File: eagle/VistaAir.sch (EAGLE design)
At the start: 11 parts, among them IC1 MCP170312MB, J1 POWER_JACK

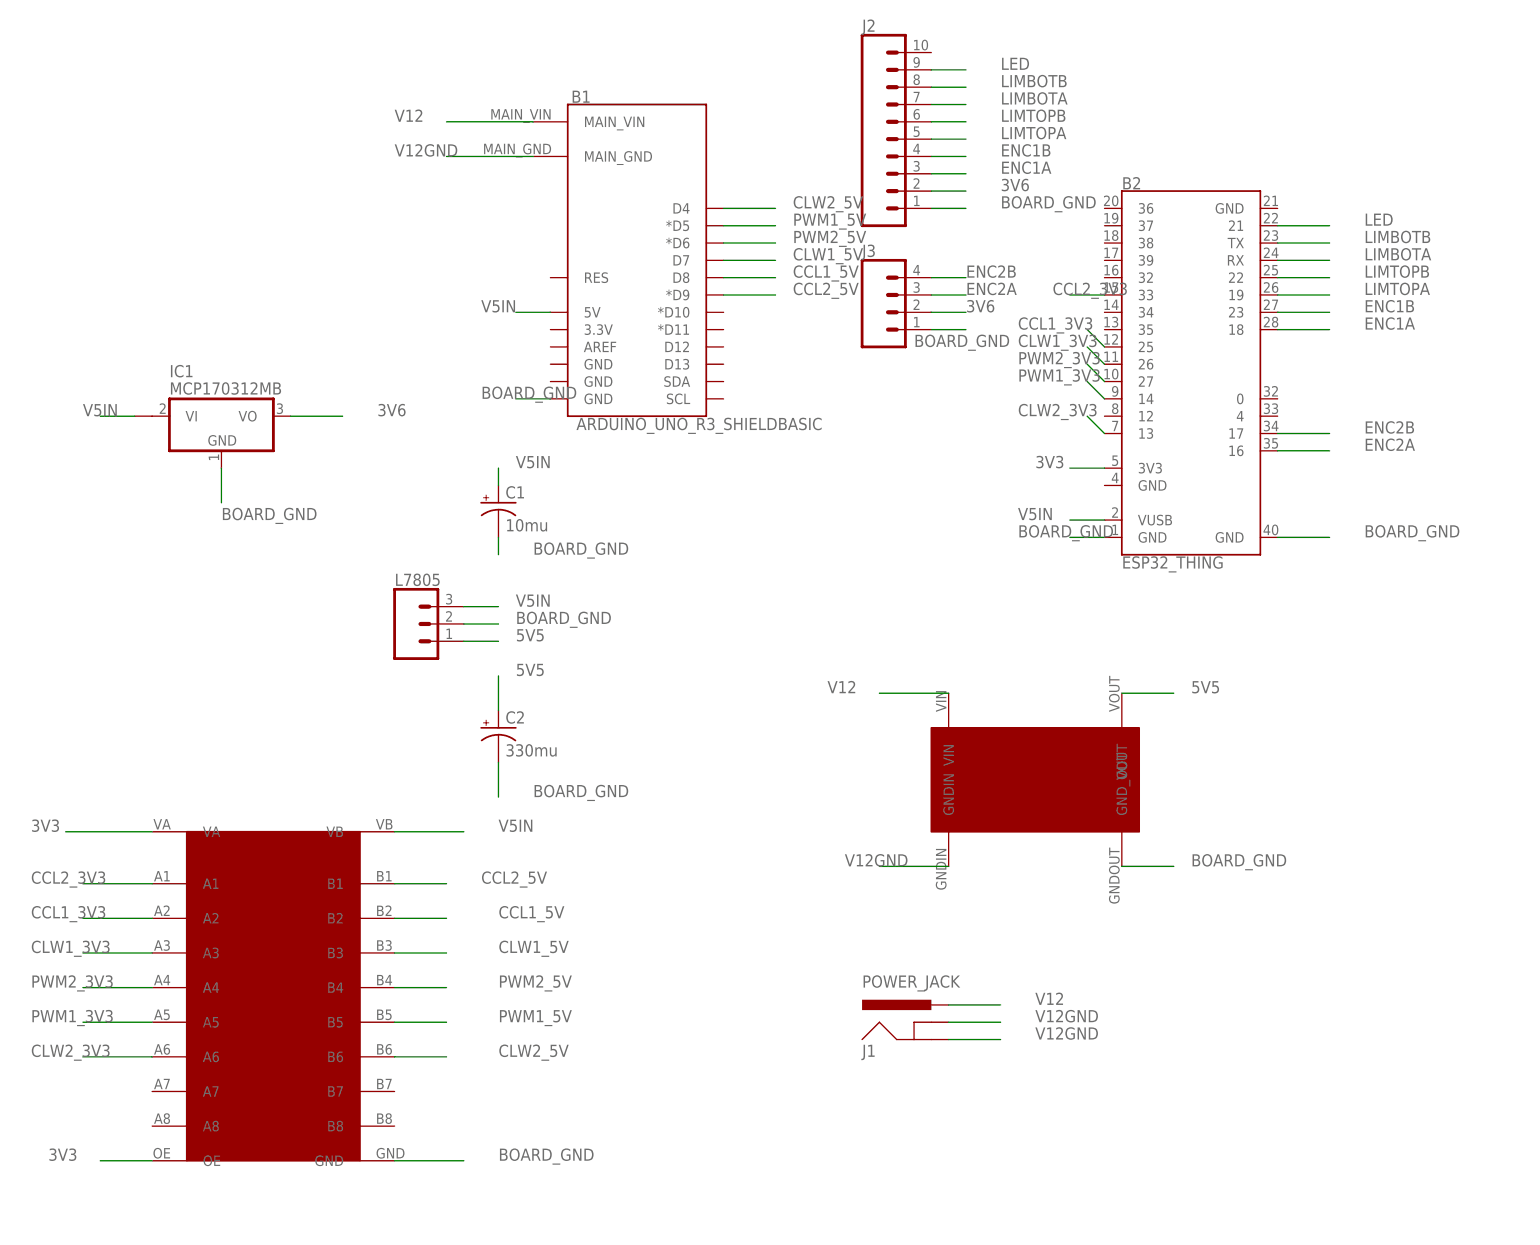
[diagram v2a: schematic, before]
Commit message: using one way logic translator since motor driver PWM inputs are open drain - and sets up ultra-high-frequency push pull with bi-directional logic shifter
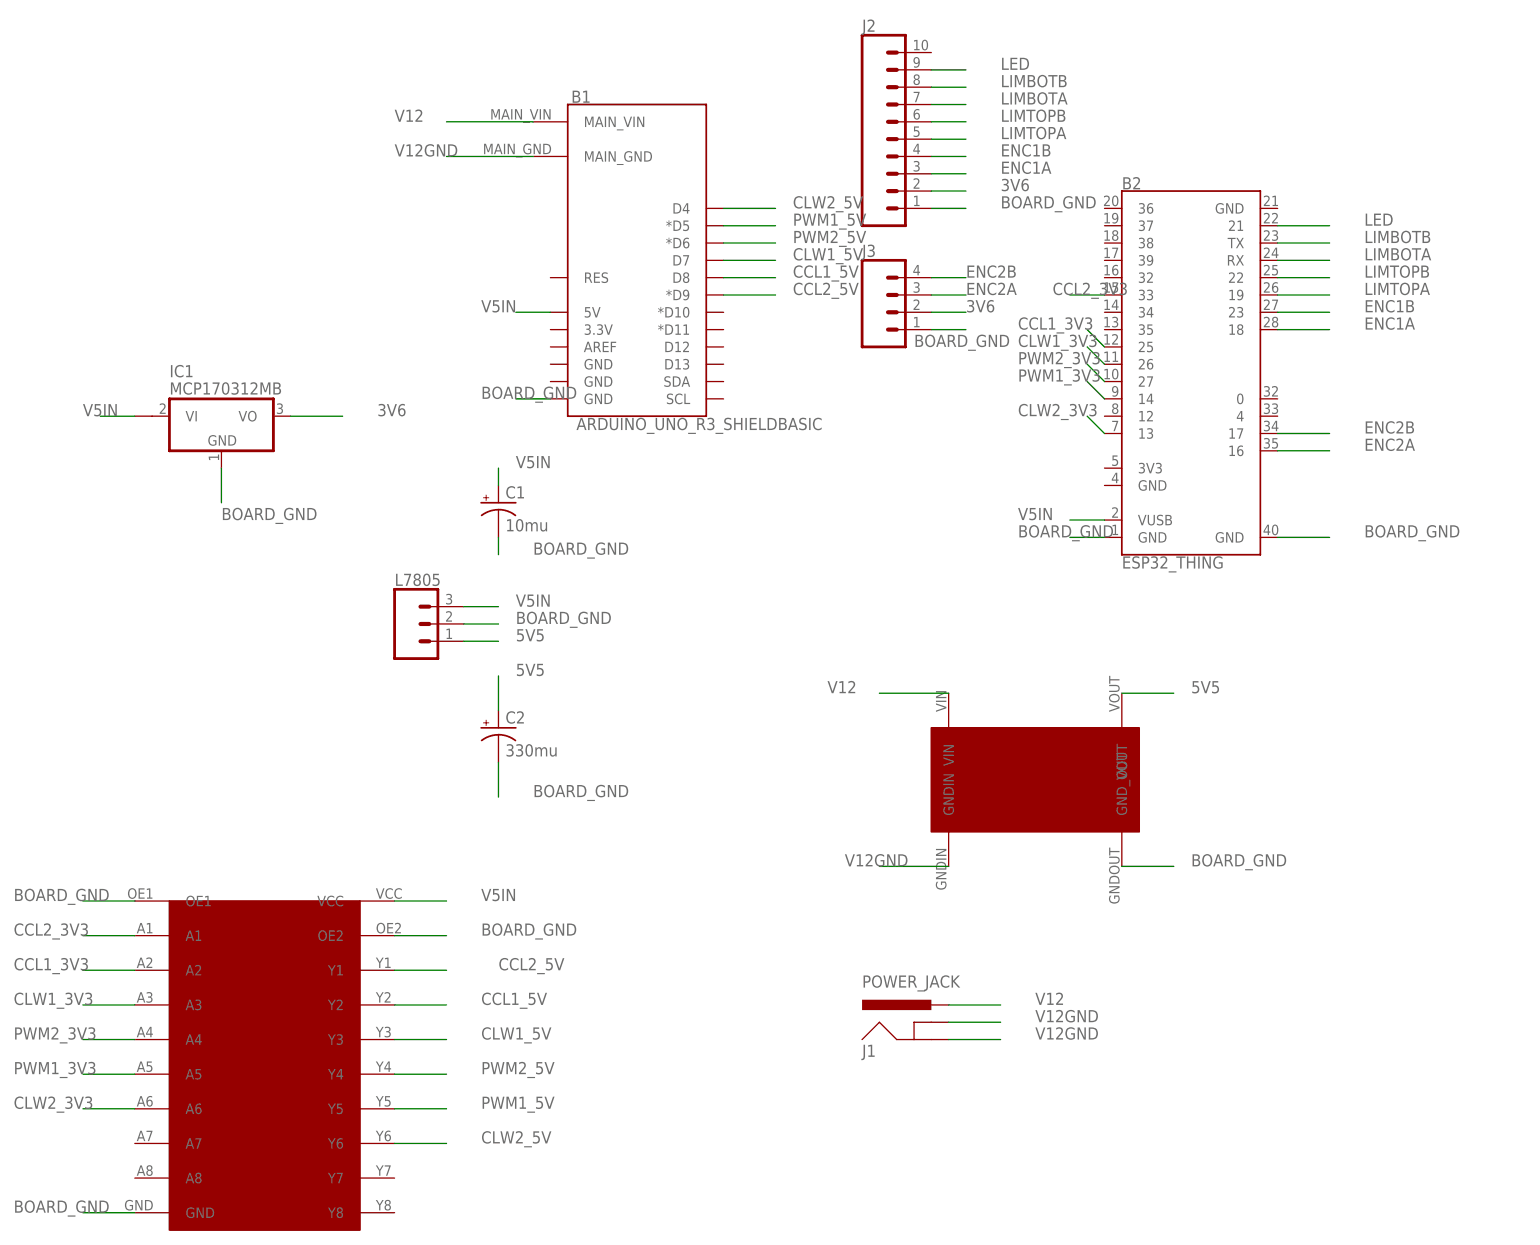
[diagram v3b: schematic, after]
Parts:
- removed U$3: 8_CHANNEL_LOGIC_CONVERTER, kevins_parts:8_CHANNEL_LOGIC_CONVERTER
- added U$1: SN74AHCT541_SOIC-20, kevins_parts:SN74AHCT541_SOIC-20
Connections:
- removed net 3V3: B2.3V3@5, U$3.OE, U$3.VA
- net BOARD_GND: now also U$1.GND, U$1.OE1, U$1.OE2; no longer U$3.GND
- net CCL1_3V3: now also U$1.A2; no longer U$3.A2
- net CCL1_5V: now also U$1.Y2; no longer U$3.B2
- net CCL2_3V3: now also U$1.A1; no longer U$3.A1
- net CCL2_5V: now also U$1.Y1; no longer U$3.B1
- net CLW1_3V3: now also U$1.A3; no longer U$3.A3
- net CLW1_5V: now also U$1.Y3; no longer U$3.B3
- net CLW2_3V3: now also U$1.A6; no longer U$3.A6
- net CLW2_5V: now also U$1.Y6; no longer U$3.B6
- net PWM1_3V3: now also U$1.A5; no longer U$3.A5
- net PWM1_5V: now also U$1.Y5; no longer U$3.B5
- net PWM2_3V3: now also U$1.A4; no longer U$3.A4
- net PWM2_5V: now also U$1.Y4; no longer U$3.B4
- net V5IN: now also U$1.VCC; no longer U$3.VB
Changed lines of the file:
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@@
 <part name="C1" library="adafruit" deviceset="CPOL-US" device="TT2D5" value="10mu"/>
 <part name="U$2" library="kevins_parts" deviceset="LM2596_STEPDOWN_MODULE" device=""/>
-<part name="U$3" library="kevins_parts" deviceset="8_CHANNEL_LOGIC_CONVERTER" device=""/>
 <part name="IC1" library="linear" deviceset="MCP1703*" device="MB" technology="12"/>
 <part name="J1" library="SparkFun-Connectors" deviceset="POWER_JACK" device=""/>
+<part name="U$1" library="kevins_parts" deviceset="SN74AHCT541_SOIC-20" device=""/>
 </parts>
 <sheets>
@@
 <instance part="C1" gate="G$1" x="25.4" y="40.64"/>
 <instance part="U$2" gate="G$1" x="99.06" y="-27.94" rot="R270"/>
-<instance part="U$3" gate="G$1" x="5.08" y="-35.56"/>
 <instance part="IC1" gate="G$1" x="-15.24" y="53.34"/>
 <instance part="J1" gate="G$1" x="88.9" y="-40.64"/>
+<instance part="U$1" gate="G$1" x="2.54" y="-43.18"/>
 </instances>
 <busses>
@@
 <net name="CLW1_3V3" class="0">
 <segment>
-<pinref part="U$3" gate="G$1" pin="A3"/>
-<wire x1="-25.4" y1="-25.4" x2="-35.56" y2="-25.4" width="0.1524" layer="91"/>
-<label x="-43.18" y="-25.4" size="1.778" layer="95"/>
-</segment>
-<segment>
 <wire x1="114.3" y1="60.96" x2="111.76" y2="63.5" width="0.1524" layer="91"/>
 <label x="101.6" y="63.5" size="1.778" layer="95"/>
 <pinref part="B2" gate="G$1" pin="26"/>
 </segment>
+<segment>
+<pinref part="U$1" gate="G$1" pin="A3"/>
+<wire x1="-27.94" y1="-33.02" x2="-35.56" y2="-33.02" width="0.1524" layer="91"/>
+<label x="-45.72" y="-33.02" size="1.778" layer="95"/>
+</segment>
 </net>
 <net name="PWM2_3V3" class="0">
-<segment>
-<pinref part="U$3" gate="G$1" pin="A4"/>
-<wire x1="-25.4" y1="-30.48" x2="-35.56" y2="-30.48" width="0.1524" layer="91"/>
-<label x="-43.18" y="-30.48" size="1.778" layer="95"/>
-</segment>
 <segment>
 <wire x1="114.3" y1="58.42" x2="111.76" y2="60.96" width="0.1524" layer="91"/>
@@
 <pinref part="B2" gate="G$1" pin="27"/>
 </segment>
+<segment>
+<pinref part="U$1" gate="G$1" pin="A4"/>
+<wire x1="-27.94" y1="-38.1" x2="-35.56" y2="-38.1" width="0.1524" layer="91"/>
+<label x="-45.72" y="-38.1" size="1.778" layer="95"/>
+</segment>
 </net>
 <net name="PWM1_3V3" class="0">
-<segment>
-<pinref part="U$3" gate="G$1" pin="A5"/>
-<wire x1="-25.4" y1="-35.56" x2="-35.56" y2="-35.56" width="0.1524" layer="91"/>
-<label x="-43.18" y="-35.56" size="1.778" layer="95"/>
-</segment>
 <segment>
 <wire x1="114.3" y1="55.88" x2="111.76" y2="58.42" width="0.1524" layer="91"/>
@@
 <pinref part="B2" gate="G$1" pin="14"/>
 </segment>
+<segment>
+<pinref part="U$1" gate="G$1" pin="A5"/>
+<wire x1="-27.94" y1="-43.18" x2="-35.56" y2="-43.18" width="0.1524" layer="91"/>
+<label x="-45.72" y="-43.18" size="1.778" layer="95"/>
+</segment>
 </net>
 <net name="CLW2_3V3" class="0">
@@
 </segment>
 <segment>
-<pinref part="U$3" gate="G$1" pin="A6"/>
-<wire x1="-25.4" y1="-40.64" x2="-35.56" y2="-40.64" width="0.1524" layer="91"/>
-<label x="-43.18" y="-40.64" size="1.778" layer="95"/>
+<pinref part="U$1" gate="G$1" pin="A6"/>
+<wire x1="-27.94" y1="-48.26" x2="-35.56" y2="-48.26" width="0.1524" layer="91"/>
+<label x="-45.72" y="-48.26" size="1.778" layer="95"/>
 </segment>
 </net>
 <net name="CCL1_3V3" class="0">
-<segment>
-<pinref part="U$3" gate="G$1" pin="A2"/>
-<wire x1="-25.4" y1="-20.32" x2="-35.56" y2="-20.32" width="0.1524" layer="91"/>
-<label x="-43.18" y="-20.32" size="1.778" layer="95"/>
-</segment>
 <segment>
 <wire x1="114.3" y1="63.5" x2="111.76" y2="66.04" width="0.1524" layer="91"/>
@@
 <pinref part="B2" gate="G$1" pin="25"/>
 </segment>
+<segment>
+<pinref part="U$1" gate="G$1" pin="A2"/>
+<wire x1="-27.94" y1="-27.94" x2="-35.56" y2="-27.94" width="0.1524" layer="91"/>
+<label x="-45.72" y="-27.94" size="1.778" layer="95"/>
+</segment>
 </net>
 <net name="CCL2_3V3" class="0">
-<segment>
-<pinref part="U$3" gate="G$1" pin="A1"/>
-<wire x1="-25.4" y1="-15.24" x2="-35.56" y2="-15.24" width="0.1524" layer="91"/>
-<label x="-43.18" y="-15.24" size="1.778" layer="95"/>
-</segment>
 <segment>
 <pinref part="B2" gate="G$1" pin="33"/>
@@
 <label x="106.68" y="71.12" size="1.778" layer="95"/>
 </segment>
+<segment>
+<pinref part="U$1" gate="G$1" pin="A1"/>
+<wire x1="-27.94" y1="-22.86" x2="-35.56" y2="-22.86" width="0.1524" layer="91"/>
+<label x="-45.72" y="-22.86" size="1.778" layer="95"/>
+</segment>
 </net>
 <net name="BOARD_GND" class="1">
@@
 </segment>
 <segment>
-<pinref part="U$3" gate="G$1" pin="GND"/>
-<wire x1="10.16" y1="-55.88" x2="20.32" y2="-55.88" width="0.1524" layer="91"/>
-<label x="25.4" y="-55.88" size="1.778" layer="95"/>
-</segment>
-<segment>
 <pinref part="IC1" gate="G$1" pin="GND"/>
 <wire x1="-15.24" y1="45.72" x2="-15.24" y2="40.64" width="0.1524" layer="91"/>
@@
 <label x="152.4" y="35.56" size="1.778" layer="95"/>
 </segment>
+<segment>
+<pinref part="U$1" gate="G$1" pin="OE1"/>
+<wire x1="-27.94" y1="-17.78" x2="-35.56" y2="-17.78" width="0.1524" layer="91"/>
+<label x="-45.72" y="-17.78" size="1.778" layer="95"/>
+</segment>
+<segment>
+<pinref part="U$1" gate="G$1" pin="OE2"/>
+<wire x1="10.16" y1="-22.86" x2="17.78" y2="-22.86" width="0.1524" layer="91"/>
+<label x="22.86" y="-22.86" size="1.778" layer="95"/>
+</segment>
+<segment>
+<pinref part="U$1" gate="G$1" pin="GND"/>
+<wire x1="-27.94" y1="-63.5" x2="-35.56" y2="-63.5" width="0.1524" layer="91"/>
+<label x="-45.72" y="-63.5" size="1.778" layer="95"/>
+</segment>
 </net>
 <net name="ENC2B" class="0">
@@
 </segment>
 <segment>
-<pinref part="U$3" gate="G$1" pin="VB"/>
-<wire x1="10.16" y1="-7.62" x2="20.32" y2="-7.62" width="0.1524" layer="91"/>
-<label x="25.4" y="-7.62" size="1.778" layer="95"/>
-</segment>
-<segment>
 <pinref part="IC1" gate="G$1" pin="VI1"/>
 <wire x1="-27.94" y1="53.34" x2="-33.02" y2="53.34" width="0.1524" layer="91"/>
@@
 <pinref part="B2" gate="G$1" pin="VUSB@2"/>
 </segment>
+<segment>
+<pinref part="U$1" gate="G$1" pin="VCC"/>
+<wire x1="10.16" y1="-17.78" x2="17.78" y2="-17.78" width="0.1524" layer="91"/>
+<label x="22.86" y="-17.78" size="1.778" layer="95"/>
+</segment>
 </net>
 <net name="LIMTOPA" class="0">
@@
 </segment>
 </net>
-<net name="3V3" class="0">
-<segment>
-<pinref part="U$3" gate="G$1" pin="VA"/>
-<wire x1="-25.4" y1="-7.62" x2="-38.1" y2="-7.62" width="0.1524" layer="91"/>
-<label x="-43.18" y="-7.62" size="1.778" layer="95"/>
-</segment>
-<segment>
-<pinref part="U$3" gate="G$1" pin="OE"/>
-<wire x1="-25.4" y1="-55.88" x2="-33.02" y2="-55.88" width="0.1524" layer="91"/>
-<label x="-40.64" y="-55.88" size="1.778" layer="95"/>
-</segment>
-<segment>
-<pinref part="B2" gate="G$1" pin="3V3@5"/>
-<wire x1="114.3" y1="45.72" x2="109.22" y2="45.72" width="0.1524" layer="91"/>
-<label x="104.14" y="45.72" size="1.778" layer="95"/>
-</segment>
-</net>
 <net name="CLW2_5V" class="0">
 <segment>
@@
 </segment>
 <segment>
-<pinref part="U$3" gate="G$1" pin="B6"/>
-<wire x1="10.16" y1="-40.64" x2="17.78" y2="-40.64" width="0.1524" layer="91"/>
-<label x="25.4" y="-40.64" size="1.778" layer="95"/>
+<pinref part="U$1" gate="G$1" pin="Y6"/>
+<wire x1="10.16" y1="-53.34" x2="17.78" y2="-53.34" width="0.1524" layer="91"/>
+<label x="22.86" y="-53.34" size="1.778" layer="95"/>
 </segment>
 </net>
@@
 </segment>
 <segment>
-<pinref part="U$3" gate="G$1" pin="B5"/>
-<wire x1="10.16" y1="-35.56" x2="17.78" y2="-35.56" width="0.1524" layer="91"/>
-<label x="25.4" y="-35.56" size="1.778" layer="95"/>
+<pinref part="U$1" gate="G$1" pin="Y5"/>
+<wire x1="10.16" y1="-48.26" x2="17.78" y2="-48.26" width="0.1524" layer="91"/>
+<label x="22.86" y="-48.26" size="1.778" layer="95"/>
 </segment>
 </net>
@@
 </segment>
 <segment>
-<pinref part="U$3" gate="G$1" pin="B4"/>
-<wire x1="10.16" y1="-30.48" x2="17.78" y2="-30.48" width="0.1524" layer="91"/>
-<label x="25.4" y="-30.48" size="1.778" layer="95"/>
+<pinref part="U$1" gate="G$1" pin="Y4"/>
+<wire x1="10.16" y1="-43.18" x2="17.78" y2="-43.18" width="0.1524" layer="91"/>
+<label x="22.86" y="-43.18" size="1.778" layer="95"/>
 </segment>
 </net>
@@
 </segment>
 <segment>
-<pinref part="U$3" gate="G$1" pin="B3"/>
-<wire x1="10.16" y1="-25.4" x2="17.78" y2="-25.4" width="0.1524" layer="91"/>
-<label x="25.4" y="-25.4" size="1.778" layer="95"/>
+<pinref part="U$1" gate="G$1" pin="Y3"/>
+<wire x1="10.16" y1="-38.1" x2="17.78" y2="-38.1" width="0.1524" layer="91"/>
+<label x="22.86" y="-38.1" size="1.778" layer="95"/>
 </segment>
 </net>
@@
 </segment>
 <segment>
-<pinref part="U$3" gate="G$1" pin="B2"/>
-<wire x1="10.16" y1="-20.32" x2="17.78" y2="-20.32" width="0.1524" layer="91"/>
-<label x="25.4" y="-20.32" size="1.778" layer="95"/>
+<pinref part="U$1" gate="G$1" pin="Y2"/>
+<wire x1="10.16" y1="-33.02" x2="17.78" y2="-33.02" width="0.1524" layer="91"/>
+<label x="22.86" y="-33.02" size="1.778" layer="95"/>
 </segment>
 </net>
@@
 </segment>
 <segment>
-<pinref part="U$3" gate="G$1" pin="B1"/>
-<wire x1="10.16" y1="-15.24" x2="17.78" y2="-15.24" width="0.1524" layer="91"/>
-<label x="22.86" y="-15.24" size="1.778" layer="95"/>
-</segment>
-</net>
+<pinref part="U$1" gate="G$1" pin="Y1"/>
+<wire x1="10.16" y1="-27.94" x2="17.78" y2="-27.94" width="0.1524" layer="91"/>
+<label x="25.4" y="-27.94" size="1.778" layer="95"/>
+</segment>
+</net>
